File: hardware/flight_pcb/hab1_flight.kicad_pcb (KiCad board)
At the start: 4 copper layers, 95.9 x 90.2 mm, 56 parts, among them J1 BATTERY 4xL91, J10 OLED SSD1306 (bench), J2 POWER SWITCH (on the box), J3 STDC14 SWD+VCP, J4 SPI FLASH module, J5 IMU GY-601N1, J6 BAROMETER BMP390, J7 GPS MAX-M10S, J8 DS18B20 probe, J9 LoRa E22-400M22S (adapter), Q1 AO3401A, SW1 RESET, U1 STM32G474RET6, U2 MIC5219-3.3

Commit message: hardware: barometer and GPS sockets from the real module pinouts (HW-24)
BMP390 module has 7 pins: INT CS SDO SDI SCK VCC GND (was 6 guessed).
MAX-M10S module has 5 pins: VCC GND TX RX PPS (was 4); PPS goes to PA8
(TIM1_CH1) for precise time. ERC 0, netlist check 0 mismatches, PCB
schematic parity 0; 121 unrouted connections as expected.

Co-Authored-By: Claude Opus 5.5 (1M context) <noreply@anthropic.com>
Claude-Session: https://claude.ai/code/session_01Y9WTd2yaDzj6r4py6E8uJo
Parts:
- J6: footprint Connector_PinSocket_2.54mm:PinSocket_1x06_P2.54mm_Vertical -> Connector_PinSocket_2.54mm:PinSocket_1x07_P2.54mm_Vertical
- J7: footprint Connector_PinSocket_2.54mm:PinSocket_1x04_P2.54mm_Vertical -> Connector_PinSocket_2.54mm:PinSocket_1x05_P2.54mm_Vertical
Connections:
- J6 pad 1: +3V3 -> unconnected-(J6-Pin_1-Pad1)
- J6 pad 2: GND -> +3V3
- J6 pad 3: /I2C_SCL -> +3V3
- J6 pad 5: +3V3 -> /I2C_SCL
- U1 pad 42: unconnected-(U1-PA8-Pad42) -> /GPS_PPS

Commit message: hardware: recovery buzzer on PB4 (HW-24)
Active piezo buzzer on a 2-pin JST cable to the box wall, switched on the
low side by an AO3400A from the battery rail (loud), 100k gate pull-down so
it stays silent during boot, 1N4148W in case a magnetic buzzer is used.
ERC 0, netlist check 0 mismatches, PCB parity 0.

Co-Authored-By: Claude Opus 5.5 (1M context) <noreply@anthropic.com>
Claude-Session: https://claude.ai/code/session_01Y9WTd2yaDzj6r4py6E8uJo
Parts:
- added D3: 1N4148W, Diode_SMD:D_SOD-123, F.Cu at (141.0, 184.0)
- added J11: BUZZER (+ / -), Connector_JST:JST_XH_B2B-XH-A_1x02_P2.50mm_Vertical, F.Cu at (130.0, 186.0)
- added Q2: AO3400A, Package_TO_SOT_SMD:SOT-23, F.Cu at (137.0, 181.0)
- added R12: 100k, Resistor_SMD:R_0603_1608Metric, F.Cu at (137.0, 177.0)
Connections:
- U1 pad 57: unconnected-(U1-PB4-Pad57) -> /BUZZER

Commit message: hardware: flight board routed with Freerouting (HW-24)
route_pcb.py: In1/In2 as GND/+3V3 planes, 0.5 mm tracks for the battery
and buzzer nets, a fan-out via from every SMD GND/3V3 pad to its plane
(straight out along QFP pins, a tie to a same-net pad where there is no
room), plane clearance 0.2 mm, then Freerouting (100 passes) and SES import.
gen_pcb.py: VDDA filter (FB1, C11, C12) moved under the VDDA pins, hole
labels hidden, title moved off J11; --force to re-place a routed board.

Result: 486 track segments (2.3 m), 108 vias; DRC 0 unconnected, 0
clearance errors, 0 schematic parity issues; 13 silkscreen warnings
(text over pads / neighbouring labels), cosmetic.

Co-Authored-By: Claude Opus 5.5 (1M context) <noreply@anthropic.com>
Claude-Session: https://claude.ai/code/session_01Y9WTd2yaDzj6r4py6E8uJo
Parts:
- moved C12 19.0 mm to (151.5, 156.5)
- moved C11 17.0 mm to (153.5, 156.5)
- moved FB1 15.8 mm to (155.5, 156.5)
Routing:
- net /VBAT_PROT: track 0.00 -> 192.9 mm, vias 0 -> 1
- net /I2C_SDA: track 0.00 -> 113.1 mm, vias 0 -> 3
- net /USART1_TX: track 0.00 -> 112.3 mm, vias 0 -> 4
- net /I2C_SCL: track 0.00 -> 111.0 mm, vias 0 -> 3
- net /SPI3_SCK: track 0.00 -> 106.6 mm, vias 0 -> 2
- net /USART1_RX: track 0.00 -> 103.9 mm, vias 0 -> 2
- net /SPI1_SCK: track 0.00 -> 102.2 mm, vias 0 -> 2
- net /SPI2_SCK: track 0.00 -> 83.7 mm
- net /DS18B20_DQ: track 0.00 -> 70.1 mm, vias 0 -> 2
- net /NRST: track 0.00 -> 64.1 mm, vias 0 -> 2
- net /IMU_CS: track 0.00 -> 55.9 mm
- net /SPI3_MISO: track 0.00 -> 55.7 mm
- net /SPI3_MOSI: track 0.00 -> 53.8 mm
- net /SPI1_MOSI: track 0.00 -> 51.6 mm, vias 0 -> 1
- net /LORA_NSS: track 0.00 -> 50.8 mm, vias 0 -> 2
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
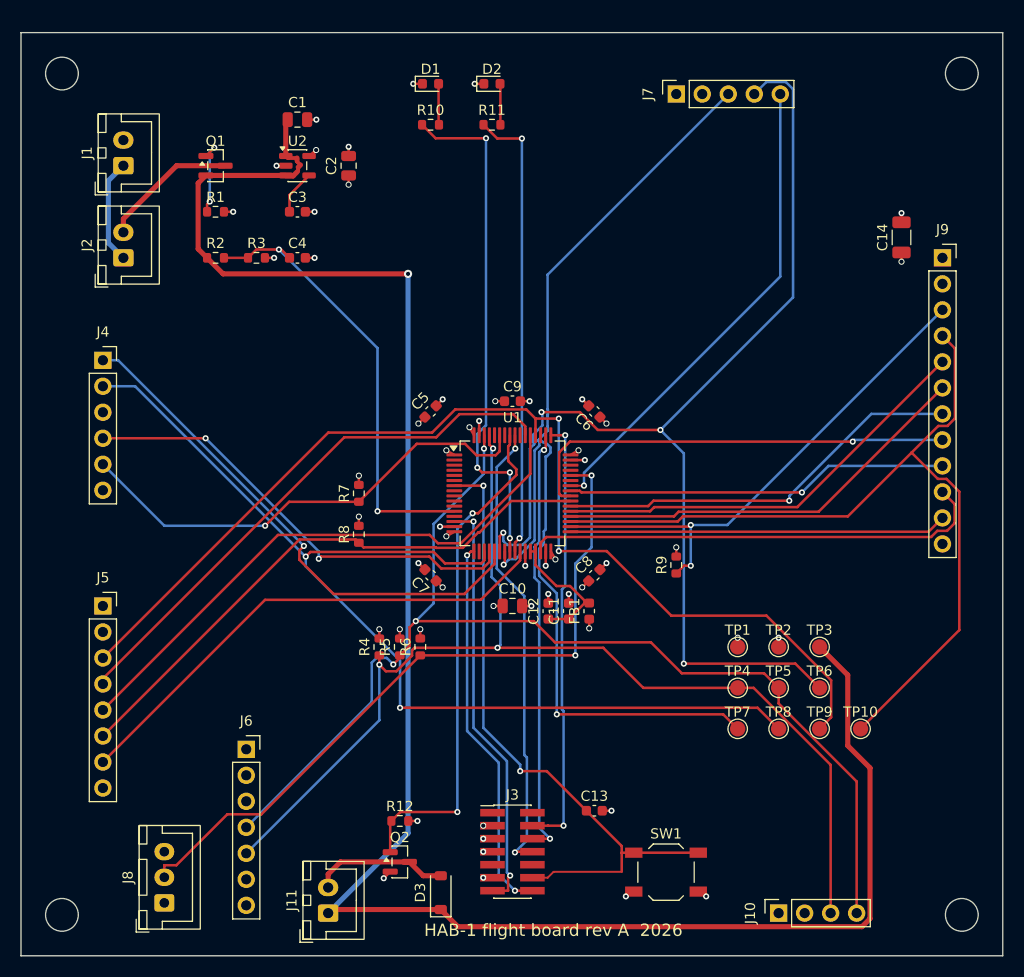
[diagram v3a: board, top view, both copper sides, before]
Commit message: flight PCB: expansion header J12 (3V3, battery rail, 4 analog pins, 2 PWM pins), rerouted
ERC 0/0, netlist check 0 mismatches, DRC 0 unconnected, 0 parity issues.

Co-Authored-By: Claude Opus 5.5 (1M context) <noreply@anthropic.com>
Claude-Session: https://claude.ai/code/session_01Y9WTd2yaDzj6r4py6E8uJo
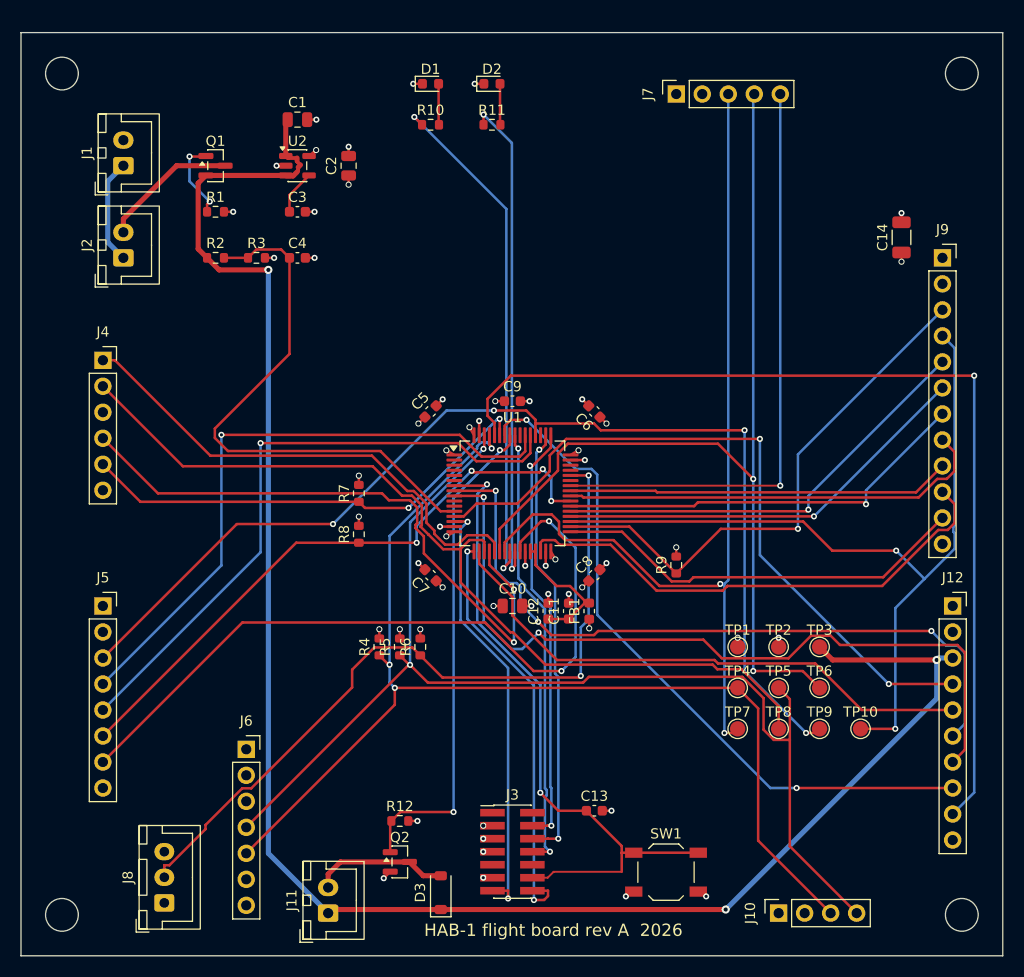
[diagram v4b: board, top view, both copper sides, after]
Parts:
- added J12: EXPANSION, Connector_PinSocket_2.54mm:PinSocket_1x10_P2.54mm_Vertical, F.Cu at (191.0, 156.0)
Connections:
- U1 pad 13: unconnected-(U1-PA1-Pad13) -> /EXP_A1
- U1 pad 18: unconnected-(U1-PA4-Pad18) -> /EXP_A2
- U1 pad 58: unconnected-(U1-PB5-Pad58) -> /EXP_PWM1
- U1 pad 60: unconnected-(U1-PB7-Pad60) -> /EXP_PWM2
- U1 pad 8: unconnected-(U1-PC0-Pad8) -> /EXP_A3
- U1 pad 9: unconnected-(U1-PC1-Pad9) -> /EXP_A4
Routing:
- net /EXP_PWM2: track 0.00 -> 96.0 mm, vias 0 -> 1
- net /EXP_A4: track 0.00 -> 77.6 mm, vias 0 -> 2
- net /EXP_A3: track 0.00 -> 70.9 mm, vias 0 -> 3
- net /EXP_A1: track 0.00 -> 69.3 mm, vias 0 -> 2
- net /EXP_PWM1: track 0.00 -> 67.8 mm, vias 0 -> 2
- net /EXP_A2: track 0.00 -> 54.4 mm
- net /IMU_INT1: track 49.8 -> 73.3 mm, vias 0 -> 2
- net /USART1_TX: track 112.3 -> 96.4 mm, vias 4 -> 2
- net /SPI1_MISO: track 44.9 -> 60.6 mm
- net /SPI1_SCK: track 102.2 -> 88.2 mm, vias 2 -> 0
- net /USART1_RX: track 103.9 -> 91.2 mm
- net /VBAT_PROT: track 192.9 -> 181.5 mm, vias 1 -> 3
- net /GPS_PPS: track 47.5 -> 58.7 mm
- net /VBAT_SENSE: track 44.1 -> 54.0 mm, vias 2 -> 0
- net /SPI3_MOSI: track 53.8 -> 61.5 mm, vias 0 -> 1
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
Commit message: flight PCB: fix swapped console TX/RX on the STDC14 connector, buzzer gate pull-down 4.7k; add the independent review report (HW-153)
Review finding B1: STDC14 pin 13 is the target RX (PA3), pin 14 the target TX (PA2).
ERC 0/0, netlist 0 mismatches, DRC 0 unconnected, 0 parity issues.

Co-Authored-By: Claude Opus 5.5 (1M context) <noreply@anthropic.com>
Claude-Session: https://claude.ai/code/session_01Y9WTd2yaDzj6r4py6E8uJo
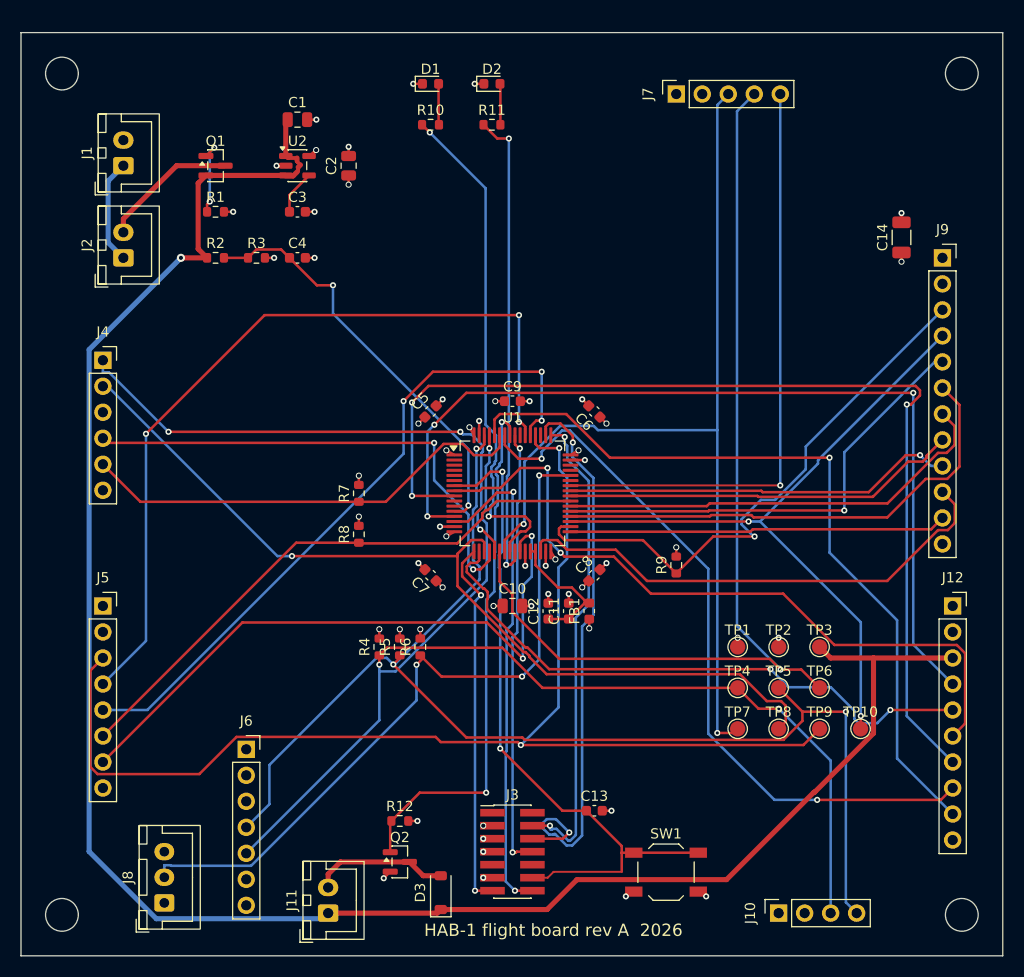
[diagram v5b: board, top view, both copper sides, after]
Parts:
- R12: value 100k -> 4.7k
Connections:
- J3 pad 13: /VCP_TX -> /VCP_RX
- J3 pad 14: /VCP_RX -> /VCP_TX
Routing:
- net /EXP_A4: track 77.6 -> 102.7 mm, vias 2 -> 3
- net /EXP_A1: track 69.3 -> 90.0 mm, vias 2 -> 3
- net /EXP_PWM2: track 96.0 -> 76.0 mm
- net /SPI3_MOSI: track 61.5 -> 79.5 mm, vias 1 -> 3
- net /VBAT_PROT: track 181.5 -> 196.2 mm, vias 3 -> 1
- net /SWCLK: track 43.3 -> 57.1 mm
- net /SPI2_SCK: track 81.7 -> 68.4 mm
- net /VBAT_SENSE: track 54.0 -> 41.1 mm, vias 0 -> 2
- net /SPI1_MISO: track 60.6 -> 49.3 mm
- net /SPI3_SCK: track 108.4 -> 119.7 mm, vias 4 -> 2
- net /IMU_INT1: track 73.3 -> 62.7 mm
- net /I2C_SDA: track 116.9 -> 124.1 mm, vias 2 -> 3
- net /SPI2_MISO: track 41.5 -> 48.6 mm, vias 1 -> 0
- net /VCP_TX: track 42.6 -> 48.3 mm
- net /SWDIO: track 41.8 -> 47.1 mm
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
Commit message: flight PCB: review fixes - fuses, cable protection, SCL off the BOOT0 pin, decoupling at the pins, silkscreen pin names (HW-153)
F1/F2 resettable fuses, series resistors on the DS18B20 cable and the expansion
header, I2C SCL moved PB8 -> PA15 with PB8 pulled down, 100 nF 2 mm from each VDD
pin and at NRST / VDDA, pull-downs on LORA_TXEN/RXEN, module and pin names on silk.
ERC 0/0, netlist 0 mismatches, DRC 0 unconnected, 0 parity issues.

Co-Authored-By: Claude Opus 5.5 (1M context) <noreply@anthropic.com>
Claude-Session: https://claude.ai/code/session_01Y9WTd2yaDzj6r4py6E8uJo
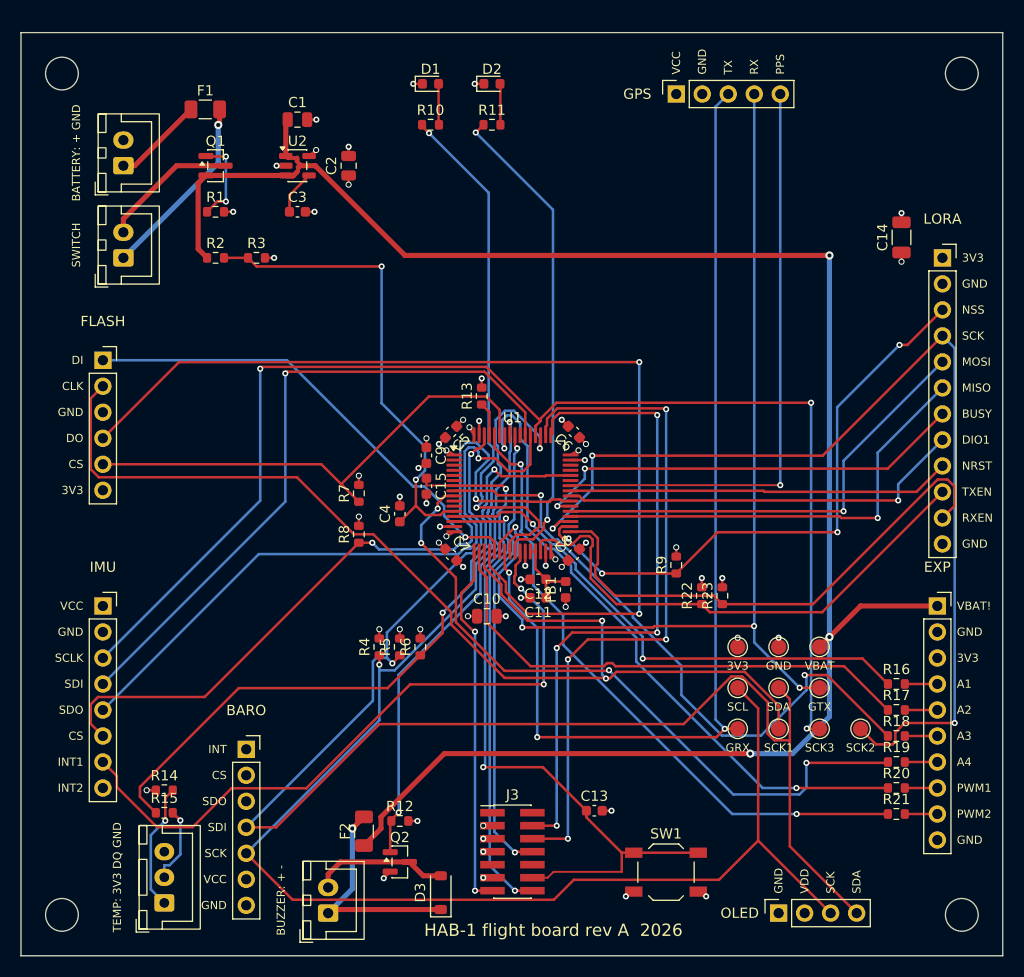
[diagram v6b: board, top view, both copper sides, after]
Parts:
- added C15: 100n, Capacitor_SMD:C_0603_1608Metric, F.Cu at (139.6, 144.3)
- added F1: PTC 0.5A hold, Fuse:Fuse_1206_3216Metric, F.Cu at (118.0, 107.5)
- added F2: PTC 0.2A hold, Fuse:Fuse_1206_3216Metric, F.Cu at (133.5, 178.0)
- added R13: 10k, Resistor_SMD:R_0603_1608Metric, F.Cu at (145.0, 135.5)
- added R14: 100, Resistor_SMD:R_0603_1608Metric, F.Cu at (114.0, 174.0)
- added R15: 100, Resistor_SMD:R_0603_1608Metric, F.Cu at (114.0, 176.2)
- added R16: 1k, Resistor_SMD:R_0603_1608Metric, F.Cu at (185.5, 163.6)
- added R17: 1k, Resistor_SMD:R_0603_1608Metric, F.Cu at (185.5, 166.2)
- added R18: 1k, Resistor_SMD:R_0603_1608Metric, F.Cu at (185.5, 168.7)
- added R19: 1k, Resistor_SMD:R_0603_1608Metric, F.Cu at (185.5, 171.2)
- added R20: 1k, Resistor_SMD:R_0603_1608Metric, F.Cu at (185.5, 173.8)
- added R21: 1k, Resistor_SMD:R_0603_1608Metric, F.Cu at (185.5, 176.3)
- added R22: 100k, Resistor_SMD:R_0603_1608Metric, F.Cu at (166.5, 155.0)
- added R23: 100k, Resistor_SMD:R_0603_1608Metric, F.Cu at (168.5, 155.0)
- moved C4 26.9 mm to (137.0, 147.0), turned to 90 degrees
- moved C9 9.93 mm to (139.6, 141.3), turned to -90 degrees
- moved C11 3.27 mm to (150.5, 155.2), turned to 180 degrees
- moved C12 3.26 mm to (150.5, 153.4), turned to 180 degrees
- moved FB1 3.11 mm to (153.2, 154.4)
- moved C5 2.83 mm to (142.0, 139.0), turned to -135 degrees
- moved C6 2.83 mm to (154.0, 139.0)
- moved C7 2.83 mm to (142.0, 151.0), turned to -45 degrees
- moved C8 2.83 mm to (154.0, 151.0)
- moved C10 2.69 mm to (145.5, 157.0)
- moved J12 1.50 mm to (189.5, 156.0)
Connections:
- D3 pad 1: /VBAT_PROT -> /BUZ_P
- J1 pad 1: /VBAT_RAW -> /VBAT_IN
- J11 pad 1: /VBAT_PROT -> /BUZ_P
- J12 pad 1: +3V3 -> /VBAT_PROT
- J12 pad 3: /VBAT_PROT -> +3V3
- J12 pad 4: /EXP_A1 -> /X_A1
- J12 pad 5: /EXP_A2 -> /X_A2
- J12 pad 6: /EXP_A3 -> /X_A3
- J12 pad 7: /EXP_A4 -> /X_A4
- J12 pad 8: /EXP_PWM1 -> /X_PWM1
- J12 pad 9: /EXP_PWM2 -> /X_PWM2
- J8 pad 1: +3V3 -> /DS_VCC
- J8 pad 2: /DS18B20_DQ -> /DS_DQ
- U1 pad 51: unconnected-(U1-PA15-Pad51) -> /I2C_SCL
- U1 pad 61: /I2C_SCL -> /BOOT0
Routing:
- net /SPI1_MISO: track 49.3 -> 98.6 mm
- net /EXP_A1: track 90.0 -> 51.1 mm, vias 3 -> 2
- net /EXP_A4: track 102.7 -> 67.6 mm, vias 3 -> 4
- net /SPI2_SCK: track 68.4 -> 99.3 mm, vias 2 -> 3
- net /I2C_SCL: track 117.4 -> 143.8 mm, vias 3 -> 2
- net /SPI1_SCK: track 88.3 -> 110.5 mm, vias 1 -> 2
- net /BUZ_P: track 0.00 -> 22.0 mm, vias 0 -> 1
- net /IMU_CS: track 55.5 -> 75.3 mm, vias 0 -> 2
- net /I2C_SDA: track 124.1 -> 140.6 mm, vias 3 -> 2
- net /SWDIO: track 47.1 -> 63.6 mm, vias 2 -> 4
- net /LORA_RXEN: track 36.9 -> 51.9 mm
- net /SPI3_MOSI: track 79.5 -> 65.1 mm, vias 3 -> 1
- net /EXP_PWM2: track 76.0 -> 62.5 mm, vias 1 -> 2
- net /DS_VCC: track 0.00 -> 12.4 mm, vias 0 -> 1
- net /SWCLK: track 57.1 -> 67.6 mm, vias 2 -> 4
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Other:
- board text added: "3V3"
- board text added: "A1"
- board text added: "A2"
- board text added: "A3"
- board text added: "A4"
- board text added: "BARO"
- board text added: "BATTERY: + GND"
- board text added: "BUSY"
- board text added: "BUZZER: + -"
- board text added: "CLK"
- board text added: "CS"
- board text added: "DI"
- board text added: "DIO1"
- board text added: "DO"
- board text added: "EXP"
- board text added: "FLASH"
- board text added: "GND"
- board text added: "GPS"
- board text added: "GRX"
- board text added: "GTX"
- board text added: "IMU"
- board text added: "INT"
- board text added: "INT1"
- board text added: "INT2"
- board text added: "LORA"
- board text added: "MISO"
- board text added: "MOSI"
- board text added: "NRST"
- board text added: "NSS"
- board text added: "OLED"
- board text added: "PPS"
- board text added: "PWM1"
- board text added: "PWM2"
- board text added: "RX"
- board text added: "RXEN"
- board text added: "SCK"
- board text added: "SCK1"
- board text added: "SCK2"
- board text added: "SCK3"
- board text added: "SCL"
- board text added: "SCLK"
- board text added: "SDA"
- board text added: "SDI"
- board text added: "SDO"
- board text added: "SWITCH"
- board text added: "TEMP: 3V3 DQ GND"
- board text added: "TX"
- board text added: "TXEN"
- board text added: "VBAT"
- board text added: "VBAT!"
- board text added: "VCC"
- board text added: "VDD"
